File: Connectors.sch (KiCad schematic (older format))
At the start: 4 parts

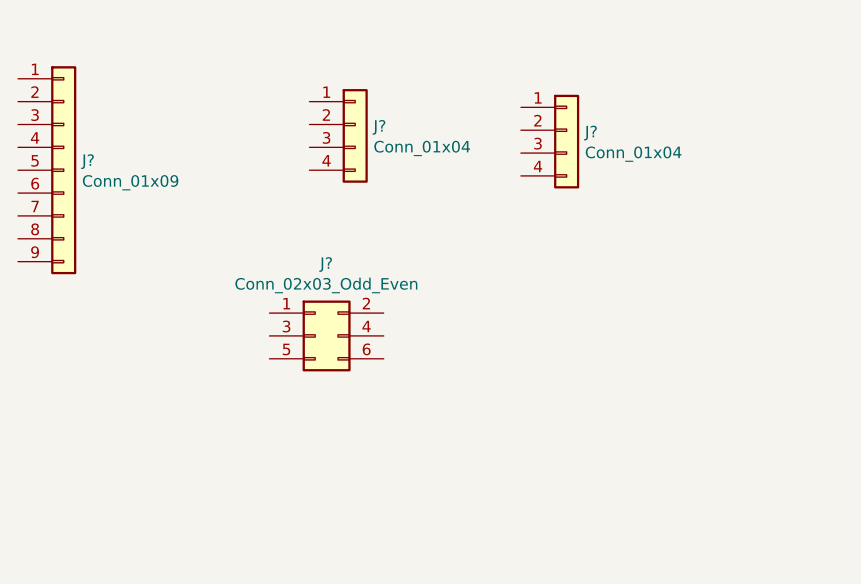
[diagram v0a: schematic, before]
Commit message: Arranged symbols appropriately
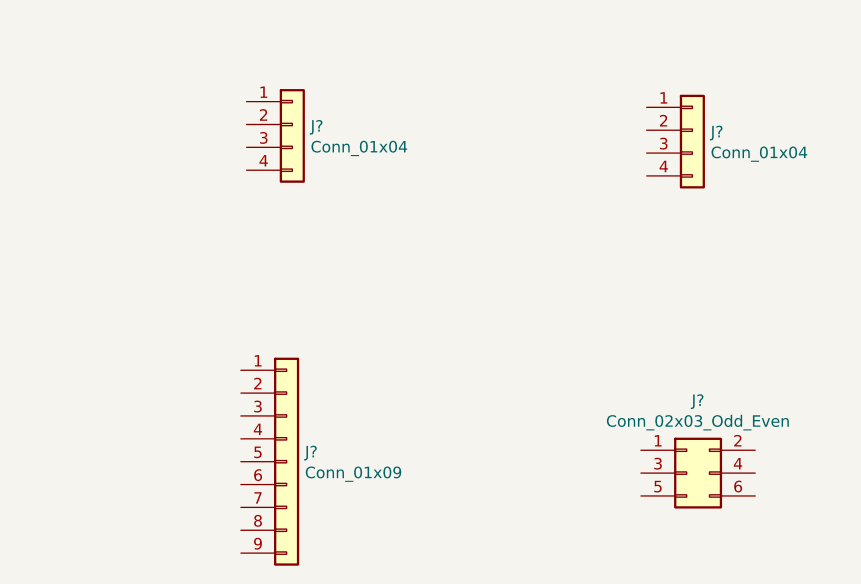
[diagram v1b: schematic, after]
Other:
- moved on the sheet: J?
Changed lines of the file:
@@
 L Connector_Generic:Conn_01x09 J?
 U 1 1 601B9E92
-P 3650 3400
-F 0 "J?" H 3730 3442 50  0000 L CNN
-F 1 "Conn_01x09" H 3730 3351 50  0000 L CNN
-F 2 "" H 3650 3400 50  0001 C CNN
-F 3 "~" H 3650 3400 50  0001 C CNN
-	1    3650 3400
+P 4625 4675
+F 0 "J?" H 4705 4717 50  0000 L CNN
+F 1 "Conn_01x09" H 4705 4626 50  0000 L CNN
+F 2 "" H 4625 4675 50  0001 C CNN
+F 3 "~" H 4625 4675 50  0001 C CNN
+	1    4625 4675
 	1    0    0    -1
 $EndComp
@@
 L Connector_Generic:Conn_01x04 J?
 U 1 1 601BA689
-P 4925 3200
-F 0 "J?" H 5005 3192 50  0000 L CNN
-F 1 "Conn_01x04" H 5005 3101 50  0000 L CNN
-F 2 "" H 4925 3200 50  0001 C CNN
-F 3 "~" H 4925 3200 50  0001 C CNN
-	1    4925 3200
+P 4650 3200
+F 0 "J?" H 4730 3192 50  0000 L CNN
+F 1 "Conn_01x04" H 4730 3101 50  0000 L CNN
+F 2 "" H 4650 3200 50  0001 C CNN
+F 3 "~" H 4650 3200 50  0001 C CNN
+	1    4650 3200
 	1    0    0    -1
 $EndComp
@@
 L Connector_Generic:Conn_02x03_Odd_Even J?
 U 1 1 601BAC99
-P 4750 4125
-F 0 "J?" H 4800 4442 50  0000 C CNN
-F 1 "Conn_02x03_Odd_Even" H 4800 4351 50  0000 C CNN
-F 2 "" H 4750 4125 50  0001 C CNN
-F 3 "~" H 4750 4125 50  0001 C CNN
-	1    4750 4125
+P 6375 4725
+F 0 "J?" H 6425 5042 50  0000 C CNN
+F 1 "Conn_02x03_Odd_Even" H 6425 4951 50  0000 C CNN
+F 2 "" H 6375 4725 50  0001 C CNN
+F 3 "~" H 6375 4725 50  0001 C CNN
+	1    6375 4725
 	1    0    0    -1
 $EndComp
@@
 L Connector_Generic:Conn_01x04 J?
 U 1 1 601BB4E4
-P 5850 3225
-F 0 "J?" H 5930 3217 50  0000 L CNN
-F 1 "Conn_01x04" H 5930 3126 50  0000 L CNN
-F 2 "" H 5850 3225 50  0001 C CNN
-F 3 "~" H 5850 3225 50  0001 C CNN
-	1    5850 3225
+P 6400 3225
+F 0 "J?" H 6480 3217 50  0000 L CNN
+F 1 "Conn_01x04" H 6480 3126 50  0000 L CNN
+F 2 "" H 6400 3225 50  0001 C CNN
+F 3 "~" H 6400 3225 50  0001 C CNN
+	1    6400 3225
 	1    0    0    -1
 $EndComp

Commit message: Annotated symbols
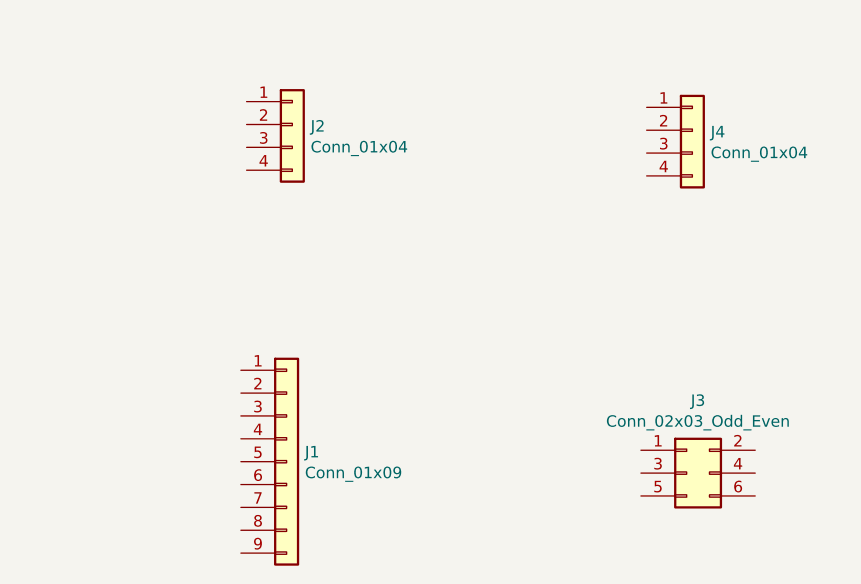
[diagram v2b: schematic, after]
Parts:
- gave numbers to parts that had none: 4
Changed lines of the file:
@@
 $EndDescr
 $Comp
-L Connector_Generic:Conn_01x09 J?
+L Connector_Generic:Conn_01x09 J1
 U 1 1 601B9E92
 P 4625 4675
-F 0 "J?" H 4705 4717 50  0000 L CNN
+F 0 "J1" H 4705 4717 50  0000 L CNN
 F 1 "Conn_01x09" H 4705 4626 50  0000 L CNN
 F 2 "" H 4625 4675 50  0001 C CNN
@@
 $EndComp
 $Comp
-L Connector_Generic:Conn_01x04 J?
+L Connector_Generic:Conn_01x04 J2
 U 1 1 601BA689
 P 4650 3200
-F 0 "J?" H 4730 3192 50  0000 L CNN
+F 0 "J2" H 4730 3192 50  0000 L CNN
 F 1 "Conn_01x04" H 4730 3101 50  0000 L CNN
 F 2 "" H 4650 3200 50  0001 C CNN
@@
 $EndComp
 $Comp
-L Connector_Generic:Conn_02x03_Odd_Even J?
+L Connector_Generic:Conn_02x03_Odd_Even J3
 U 1 1 601BAC99
 P 6375 4725
-F 0 "J?" H 6425 5042 50  0000 C CNN
+F 0 "J3" H 6425 5042 50  0000 C CNN
 F 1 "Conn_02x03_Odd_Even" H 6425 4951 50  0000 C CNN
 F 2 "" H 6375 4725 50  0001 C CNN
@@
 $EndComp
 $Comp
-L Connector_Generic:Conn_01x04 J?
+L Connector_Generic:Conn_01x04 J4
 U 1 1 601BB4E4
 P 6400 3225
-F 0 "J?" H 6480 3217 50  0000 L CNN
+F 0 "J4" H 6480 3217 50  0000 L CNN
 F 1 "Conn_01x04" H 6480 3126 50  0000 L CNN
 F 2 "" H 6400 3225 50  0001 C CNN

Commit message: Assigned footprints to symbols
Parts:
- J1: footprint (none) -> Connector_PinSocket_2.54mm:PinSocket_1x09_P2.54mm_Vertical
- J2, J4: footprint (none) -> Connector_PinSocket_2.54mm:PinSocket_1x04_P2.54mm_Vertical
- J3: footprint (none) -> Connector_PinSocket_2.54mm:PinSocket_2x03_P2.54mm_Vertical
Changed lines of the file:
@@
 F 0 "J1" H 4705 4717 50  0000 L CNN
 F 1 "Conn_01x09" H 4705 4626 50  0000 L CNN
-F 2 "" H 4625 4675 50  0001 C CNN
+F 2 "Connector_PinSocket_2.54mm:PinSocket_1x09_P2.54mm_Vertical" H 4625 4675 50  0001 C CNN
 F 3 "~" H 4625 4675 50  0001 C CNN
 	1    4625 4675
@@
 F 0 "J2" H 4730 3192 50  0000 L CNN
 F 1 "Conn_01x04" H 4730 3101 50  0000 L CNN
-F 2 "" H 4650 3200 50  0001 C CNN
+F 2 "Connector_PinSocket_2.54mm:PinSocket_1x04_P2.54mm_Vertical" H 4650 3200 50  0001 C CNN
 F 3 "~" H 4650 3200 50  0001 C CNN
 	1    4650 3200
@@
 F 0 "J3" H 6425 5042 50  0000 C CNN
 F 1 "Conn_02x03_Odd_Even" H 6425 4951 50  0000 C CNN
-F 2 "" H 6375 4725 50  0001 C CNN
+F 2 "Connector_PinSocket_2.54mm:PinSocket_2x03_P2.54mm_Vertical" H 6375 4725 50  0001 C CNN
 F 3 "~" H 6375 4725 50  0001 C CNN
 	1    6375 4725
@@
 F 0 "J4" H 6480 3217 50  0000 L CNN
 F 1 "Conn_01x04" H 6480 3126 50  0000 L CNN
-F 2 "" H 6400 3225 50  0001 C CNN
+F 2 "Connector_PinSocket_2.54mm:PinSocket_1x04_P2.54mm_Vertical" H 6400 3225 50  0001 C CNN
 F 3 "~" H 6400 3225 50  0001 C CNN
 	1    6400 3225

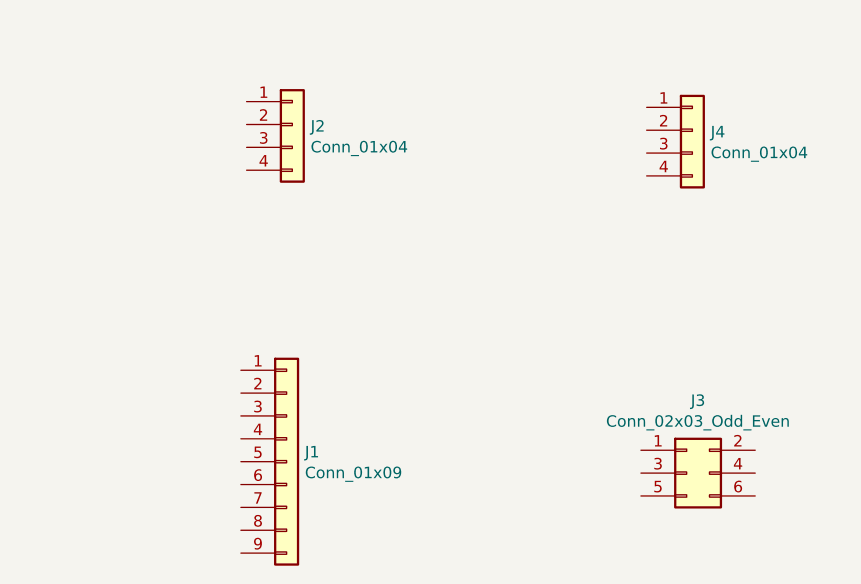
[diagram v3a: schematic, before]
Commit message: Added component values
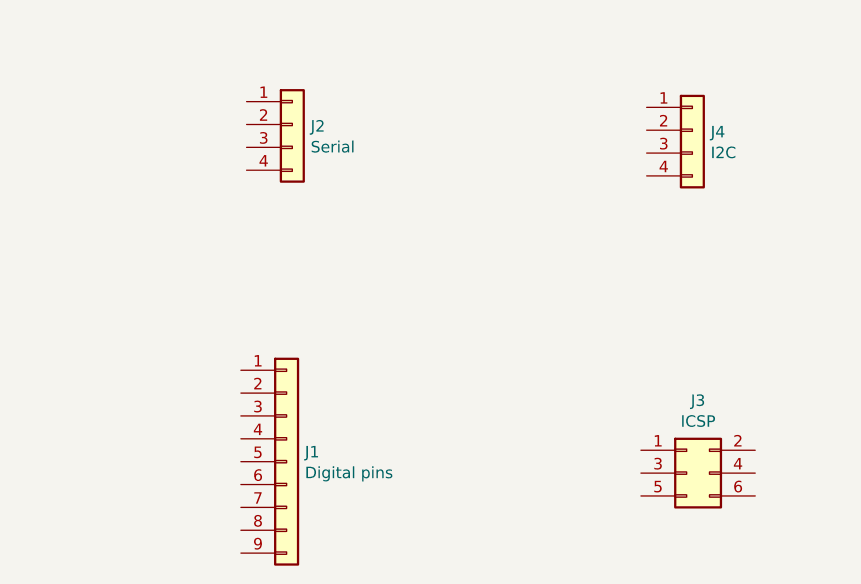
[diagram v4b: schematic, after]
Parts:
- J1: value Conn_01x09 -> Digital pins
- J2: value Conn_01x04 -> Serial
- J3: value Conn_02x03_Odd_Even -> ICSP
- J4: value Conn_01x04 -> I2C
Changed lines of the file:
@@
 P 4625 4675
 F 0 "J1" H 4705 4717 50  0000 L CNN
-F 1 "Conn_01x09" H 4705 4626 50  0000 L CNN
+F 1 "Digital pins" H 4705 4626 50  0000 L CNN
 F 2 "Connector_PinSocket_2.54mm:PinSocket_1x09_P2.54mm_Vertical" H 4625 4675 50  0001 C CNN
 F 3 "~" H 4625 4675 50  0001 C CNN
@@
 P 4650 3200
 F 0 "J2" H 4730 3192 50  0000 L CNN
-F 1 "Conn_01x04" H 4730 3101 50  0000 L CNN
+F 1 "Serial" H 4730 3101 50  0000 L CNN
 F 2 "Connector_PinSocket_2.54mm:PinSocket_1x04_P2.54mm_Vertical" H 4650 3200 50  0001 C CNN
 F 3 "~" H 4650 3200 50  0001 C CNN
@@
 P 6375 4725
 F 0 "J3" H 6425 5042 50  0000 C CNN
-F 1 "Conn_02x03_Odd_Even" H 6425 4951 50  0000 C CNN
+F 1 "ICSP" H 6425 4951 50  0000 C CNN
 F 2 "Connector_PinSocket_2.54mm:PinSocket_2x03_P2.54mm_Vertical" H 6375 4725 50  0001 C CNN
 F 3 "~" H 6375 4725 50  0001 C CNN
@@
 P 6400 3225
 F 0 "J4" H 6480 3217 50  0000 L CNN
-F 1 "Conn_01x04" H 6480 3126 50  0000 L CNN
+F 1 "I2C" H 6480 3126 50  0000 L CNN
 F 2 "Connector_PinSocket_2.54mm:PinSocket_1x04_P2.54mm_Vertical" H 6400 3225 50  0001 C CNN
 F 3 "~" H 6400 3225 50  0001 C CNN

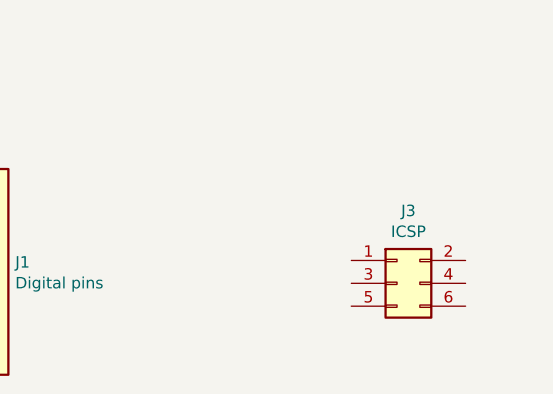
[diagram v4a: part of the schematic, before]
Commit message: Added hierarchical labels
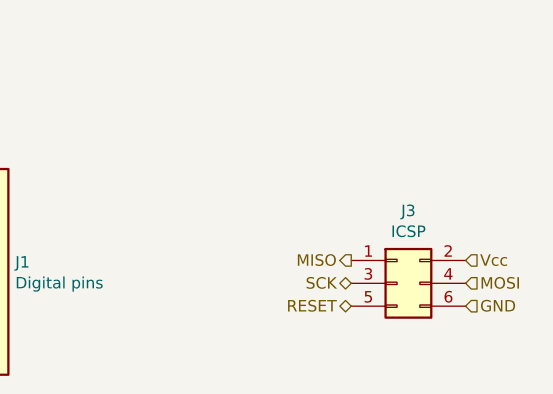
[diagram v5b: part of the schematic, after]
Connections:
- net MISO: now reaches J3.1 (Pin_1)
- net Vcc: now reaches J3.2 (Pin_2)
- net SCK: now reaches J3.3 (Pin_3)
- net MOSI: now reaches J3.4 (Pin_4)
- net RESET: now reaches J3.5 (Pin_5)
- net GND: now reaches J3.6 (Pin_6)
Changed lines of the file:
@@
 	1    0    0    -1
 $EndComp
+Text HLabel 6175 4625 0    50   Output ~ 0
+MISO
+Text HLabel 6175 4725 0    50   BiDi ~ 0
+SCK
+Text HLabel 6175 4825 0    50   BiDi ~ 0
+RESET
+Text HLabel 6675 4625 2    50   Input ~ 0
+Vcc
+Text HLabel 6675 4725 2    50   Input ~ 0
+MOSI
+Text HLabel 6675 4825 2    50   Input ~ 0
+GND
 $EndSCHEMATC

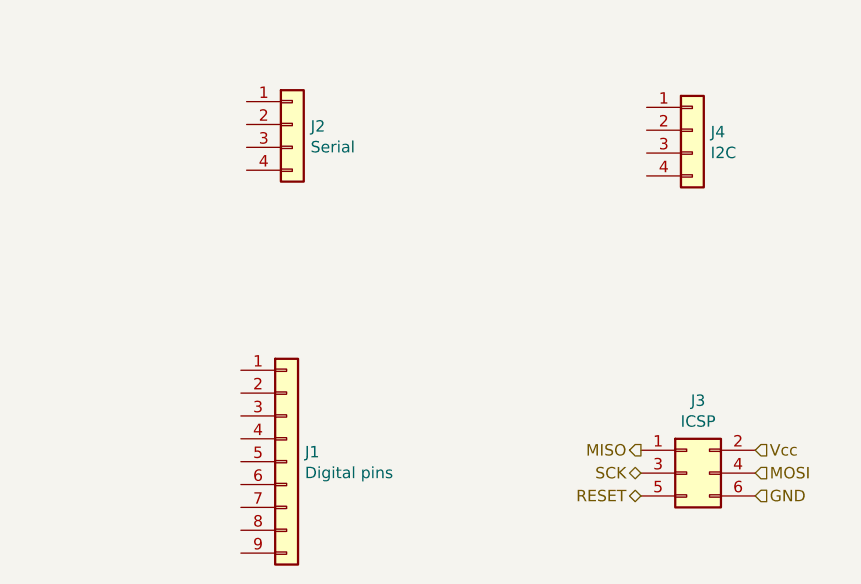
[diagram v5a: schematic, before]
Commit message: Finished hierarchical labels and root sheet connections
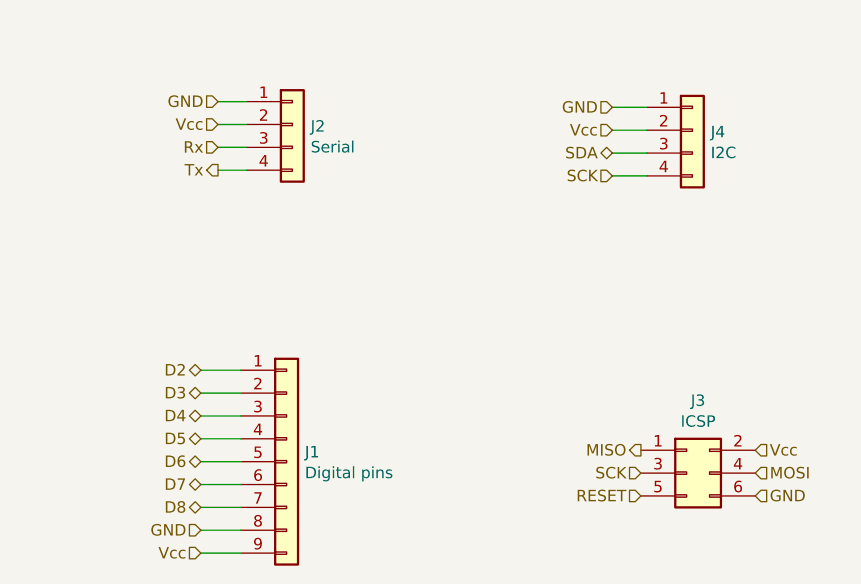
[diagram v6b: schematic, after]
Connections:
- net GND: now also J1.8 (Pin_8), J2.1 (Pin_1), J4.1 (Pin_1)
- net SCK: now also J4.4 (Pin_4)
- net Vcc: now also J1.9 (Pin_9), J2.2 (Pin_2), J4.2 (Pin_2)
- net D2: now reaches J1.1 (Pin_1)
- net D3: now reaches J1.2 (Pin_2)
- net D4: now reaches J1.3 (Pin_3)
- net D5: now reaches J1.4 (Pin_4)
- net D6: now reaches J1.5 (Pin_5)
- net D7: now reaches J1.6 (Pin_6)
- net D8: now reaches J1.7 (Pin_7)
- net Rx: now reaches J2.3 (Pin_3)
- net Tx: now reaches J2.4 (Pin_4)
- net SDA: now reaches J4.3 (Pin_3)
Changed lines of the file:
@@
 Text HLabel 6175 4625 0    50   Output ~ 0
 MISO
-Text HLabel 6175 4725 0    50   BiDi ~ 0
+Text HLabel 6175 4725 0    50   Input ~ 0
 SCK
-Text HLabel 6175 4825 0    50   BiDi ~ 0
+Text HLabel 6175 4825 0    50   Input ~ 0
 RESET
 Text HLabel 6675 4625 2    50   Input ~ 0
@@
 Text HLabel 6675 4825 2    50   Input ~ 0
 GND
+Text HLabel 4325 3100 0    50   Input ~ 0
+GND
+Text HLabel 4325 3200 0    50   Input ~ 0
+Vcc
+Text HLabel 4325 3300 0    50   Input ~ 0
+Rx
+Text HLabel 4325 3400 0    50   Output ~ 0
+Tx
+Wire Wire Line
+	4325 3100 4450 3100
+Wire Wire Line
+	4325 3200 4450 3200
+Wire Wire Line
+	4325 3300 4450 3300
+Wire Wire Line
+	4325 3400 4450 3400
+Text HLabel 6050 3125 0    50   Input ~ 0
+GND
+Text HLabel 6050 3225 0    50   Input ~ 0
+Vcc
+Text HLabel 6050 3325 0    50   BiDi ~ 0
+SDA
+Text HLabel 6050 3425 0    50   Input ~ 0
+SCK
+Wire Wire Line
+	6050 3125 6200 3125
+Wire Wire Line
+	6050 3225 6200 3225
+Wire Wire Line
+	6050 3325 6200 3325
+Wire Wire Line
+	6050 3425 6200 3425
+Text HLabel 4250 4275 0    50   BiDi ~ 0
+D2
+Text HLabel 4250 4375 0    50   BiDi ~ 0
+D3
+Text HLabel 4250 4475 0    50   BiDi ~ 0
+D4
+Text HLabel 4250 4575 0    50   BiDi ~ 0
+D5
+Text HLabel 4250 4675 0    50   BiDi ~ 0
+D6
+Text HLabel 4250 4775 0    50   BiDi ~ 0
+D7
+Text HLabel 4250 4875 0    50   BiDi ~ 0
+D8
+Text HLabel 4250 4975 0    50   Input ~ 0
+GND
+Text HLabel 4250 5075 0    50   Input ~ 0
+Vcc
+Wire Wire Line
+	4250 4275 4425 4275
+Wire Wire Line
+	4250 4375 4425 4375
+Wire Wire Line
+	4250 4475 4425 4475
+Wire Wire Line
+	4250 4575 4425 4575
+Wire Wire Line
+	4250 4675 4425 4675
+Wire Wire Line
+	4250 4775 4425 4775
+Wire Wire Line
+	4250 4875 4425 4875
+Wire Wire Line
+	4250 4975 4425 4975
+Wire Wire Line
+	4250 5075 4425 5075
 $EndSCHEMATC

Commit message: Added functional block descriptions
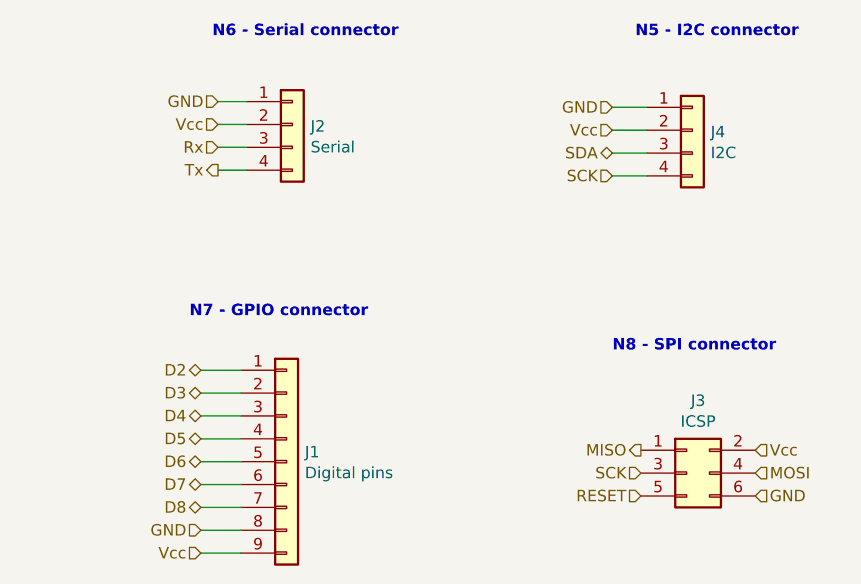
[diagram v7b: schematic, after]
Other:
- note added: "N5 - I2C connector"
- note added: "N6 - Serial connector"
- note added: "N7 - GPIO connector"
- note added: "N8 - SPI connector\n"
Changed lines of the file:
@@
 Wire Wire Line
 	4250 5075 4425 5075
+Text Notes 4300 2825 0    50   ~ 10
+N6 - Serial connector
+Text Notes 6150 2825 0    50   ~ 10
+N5 - I2C connector
+Text Notes 4200 4050 0    50   ~ 10
+N7 - GPIO connector
+Text Notes 6050 4200 0    50   ~ 10
+N8 - SPI connector\n
 $EndSCHEMATC
